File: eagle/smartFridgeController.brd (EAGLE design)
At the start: 39.7 x 25.4 mm, 8 parts

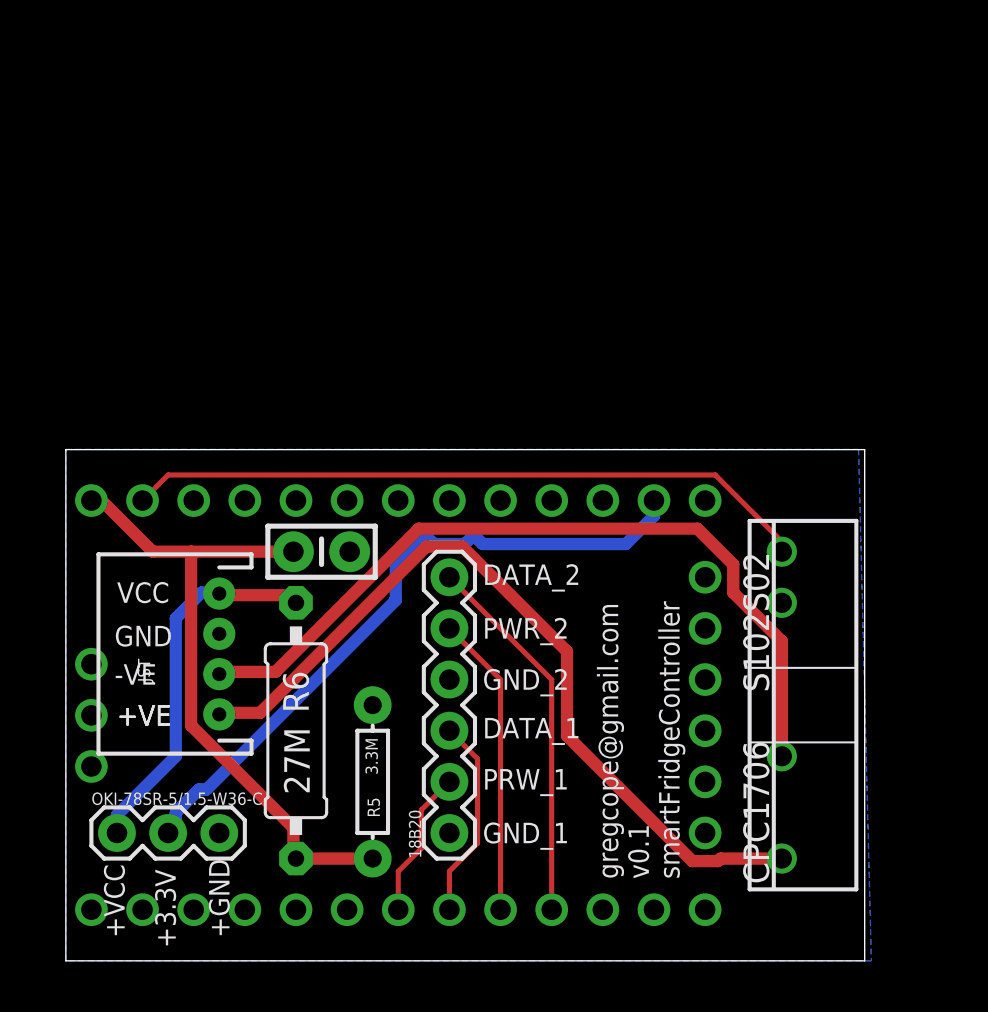
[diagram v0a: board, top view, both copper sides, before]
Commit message: added 3 LEDs
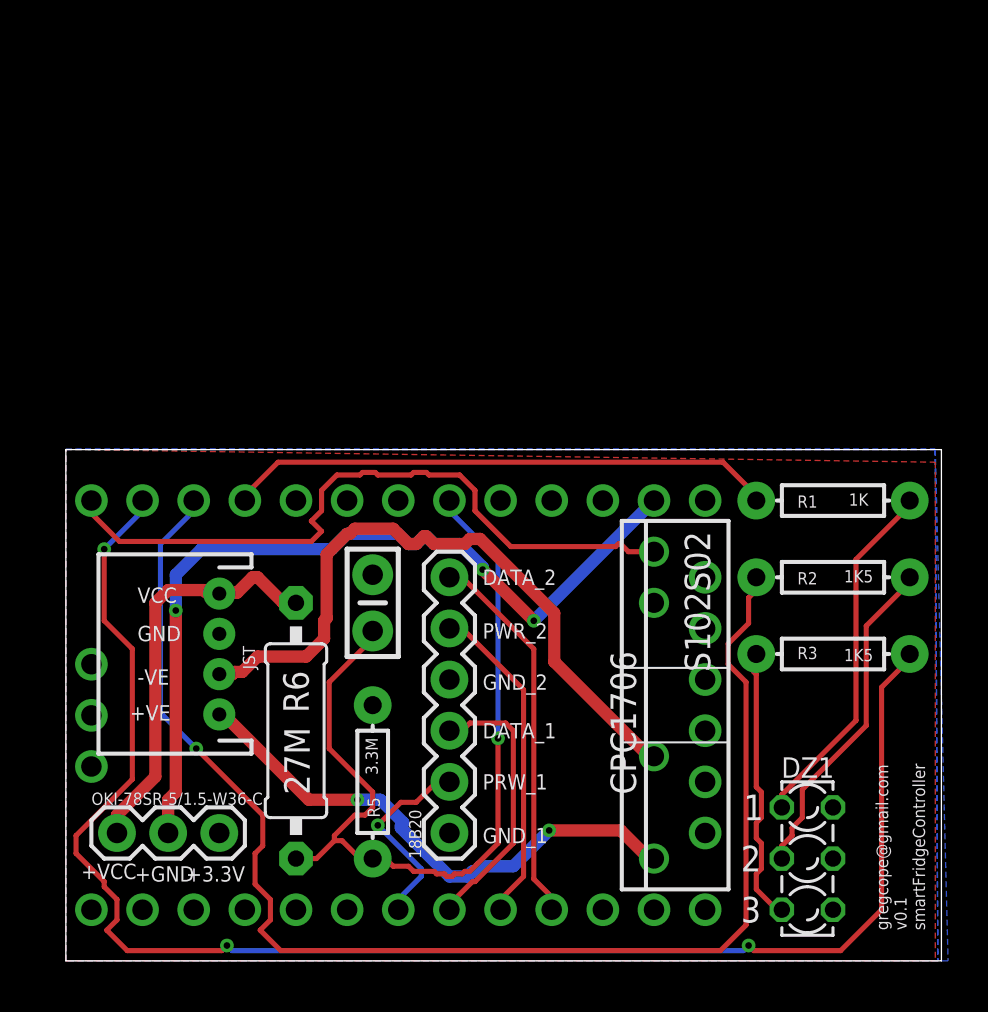
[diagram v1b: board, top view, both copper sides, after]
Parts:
- added DZ1: LZR183, led:LZR183
- added R1: 1K, SparkFun-Resistors:AXIAL-0.3
- added R2, R3: 1K5, SparkFun-Resistors:AXIAL-0.3
- moved CPC1706 6.35 mm to (29.2, 12.7)
- moved C2 3.59 mm to (15.2, 17.8), turned to 90 degrees
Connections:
- removed net A0_VCC_VD: C2.1, R5.P$2, R6.1, U$1.A0
- removed net D15_RELAY_PIN: CPC1706.4, U$1.A1
- new net A7_VCC_VD: C2.1, R5.P$2, R6.1, U$1.A7_ONLY
- new net D14_RELAY_PIN: CPC1706.4, U$1.A0
- new net D15_LED_RED_PIN: R3.P$2, U$1.A1
- new net D16_LED_YELLOW_PIN: R2.P$2, U$1.A2
- new net D17_LED_GREEN_PIN: R1.P$2, U$1.A3
- new net N$1: DZ1.A1, R1.P$1
- new net N$2: DZ1.A2, R2.P$1
- new net N$3: DZ1.A3, R3.P$1
- net GND: now also DZ1.K1, DZ1.K2, DZ1.K3
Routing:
- net D15_LED_RED_PIN: track 0.00 -> 78.4 mm, vias 0 -> 3
- net D16_LED_YELLOW_PIN: track 0.00 -> 68.1 mm, vias 0 -> 1
- net A7_VCC_VD: track 0.00 -> 43.1 mm, vias 0 -> 1
- net D14_RELAY_PIN: track 0.00 -> 34.6 mm
- net D15_RELAY_PIN: track 34.2 -> 0.00 mm
- net A0_VCC_VD: track 32.3 -> 0.00 mm
- net D17_LED_GREEN_PIN: track 0.00 -> 27.3 mm
- net N$1: track 0.00 -> 17.9 mm
- net N$2: track 0.00 -> 16.6 mm
- net N$3: track 0.00 -> 13.9 mm
- net +VE: track 40.4 -> 26.8 mm, vias 0 -> 2
- net VIN: track 33.5 -> 42.2 mm, vias 0 -> 3
- net -VE: track 39.8 -> 33.6 mm
- net D6_DS1_DATA: track 10.0 -> 13.8 mm
- net D7_DS1_PWR: track 7.40 -> 10.0 mm, vias 0 -> 1
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- added copper zone on layer 1, net GND
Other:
- board size 39.7 x 25.4 mm -> 43.5 x 25.4 mm

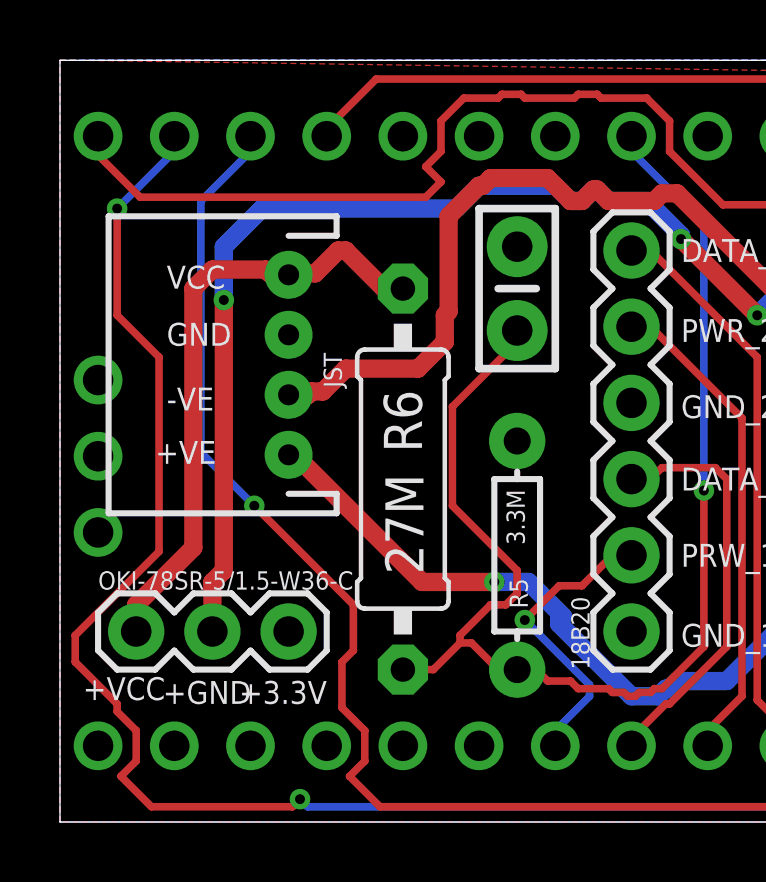
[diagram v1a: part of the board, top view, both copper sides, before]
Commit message: silkscreen updates
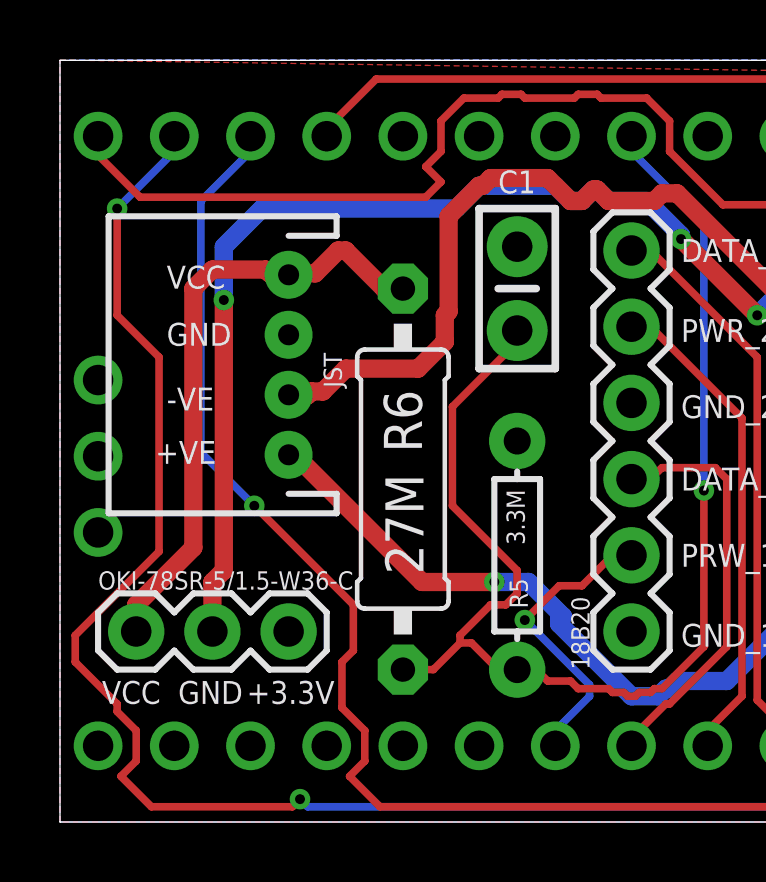
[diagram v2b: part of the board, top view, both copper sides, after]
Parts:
- renumbered C2 to C1
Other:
- board text added: "C1"
- board text removed: "+GND"
- board text removed: "+VCC"
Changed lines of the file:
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@@
 <text x="20.701" y="5.842" size="0.762" layer="25" font="vector">GND_1</text>
 <text x="3.175" y="11.938" size="0.762" layer="25" font="vector">+VE</text>
-<text x="0.762" y="4.064" size="0.762" layer="25" font="vector">+VCC</text>
-<text x="5.969" y="3.937" size="0.762" layer="25" font="vector">+3.3V</text>
-<text x="3.429" y="3.937" size="0.762" layer="25" font="vector">+GND</text>
+<text x="1.397" y="3.937" size="0.762" layer="25" font="vector">VCC</text>
+<text x="6.223" y="3.937" size="0.762" layer="25" font="vector">+3.3V</text>
+<text x="3.937" y="3.937" size="0.762" layer="25" font="vector">GND</text>
+<text x="14.605" y="20.955" size="0.762" layer="25" font="vector">C1</text>
 </plain>
 <attributes>
@@
 </autorouter>
 <elements>
-<element name="C2" library="SparkFun-Capacitors" package="CAP-PTH-SMALL-KIT" value="0.1U" x="15.24" y="17.78" smashed="yes" rot="R90">
+<element name="C1" library="SparkFun-Capacitors" package="CAP-PTH-SMALL-KIT" value="0.1U" x="15.24" y="17.78" smashed="yes" rot="R90">
 <attribute name="PROD_ID" value="CAP-08370" x="-11.43" y="6.35" size="1.778" layer="27" rot="R90" display="off"/>
 </element>
@@
 <vertex x="0" y="0"/>
 </polygon>
-<contactref element="C2" pad="2"/>
+<contactref element="C1" pad="2"/>
 <contactref element="R5" pad="P$1"/>
 <contactref element="JST" pad="3"/>
@@
 <signal name="A7_VCC_VD">
 <contactref element="U$1" pad="A7_ONLY"/>
-<contactref element="C2" pad="1"/>
+<contactref element="C1" pad="1"/>
 <contactref element="R5" pad="P$2"/>
 <contactref element="R6" pad="1"/>

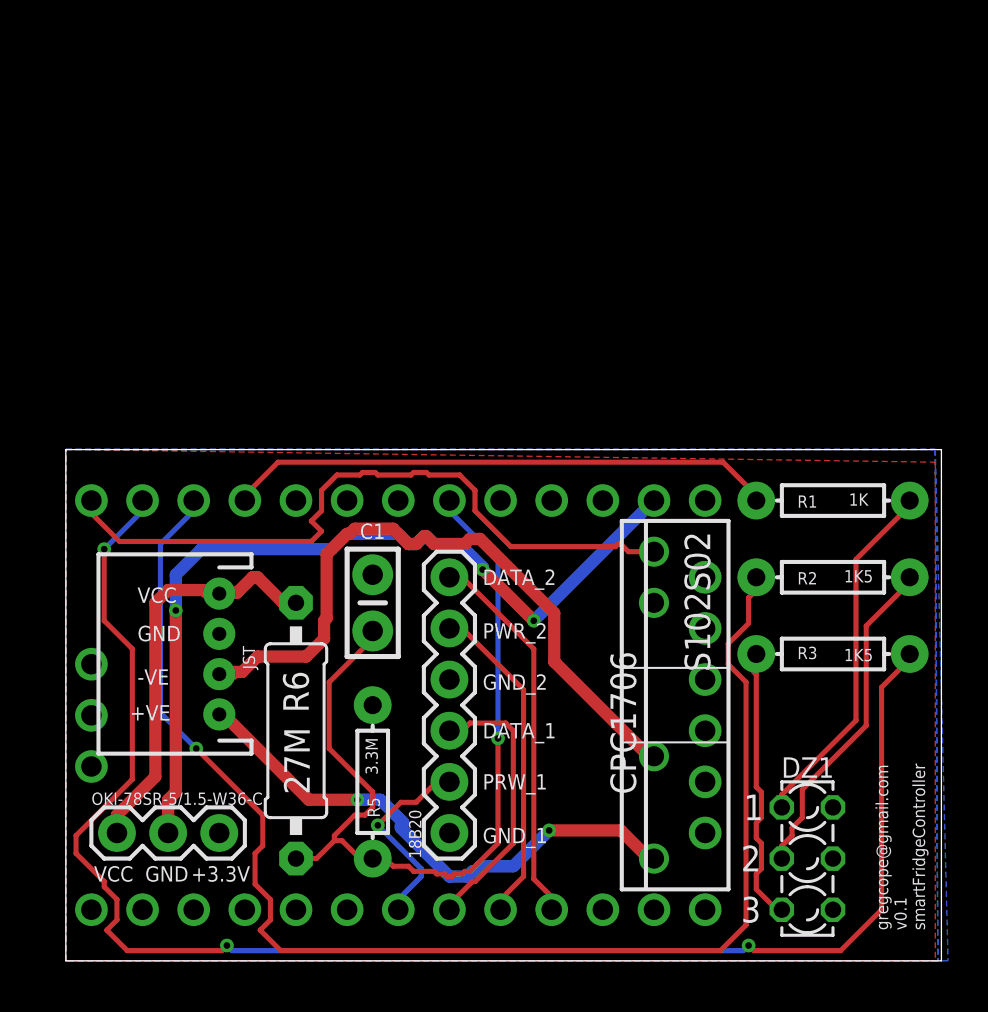
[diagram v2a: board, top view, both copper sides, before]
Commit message: Swapped IXYS pins
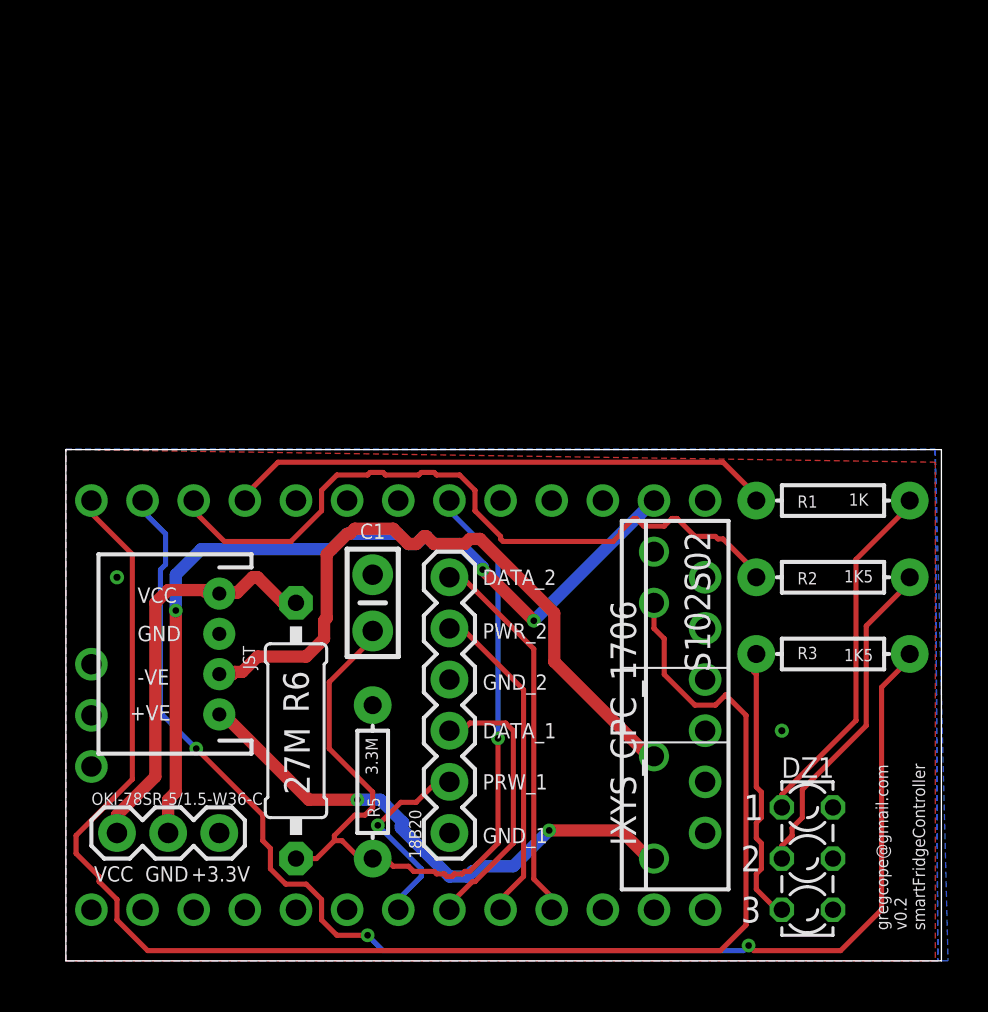
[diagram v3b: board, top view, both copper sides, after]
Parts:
- renumbered CPC1706 to IXYS_CPC_1706
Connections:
- net D14_RELAY_PIN: now also IXYS_CPC_1706.3; no longer IXYS_CPC_1706.4
- net GND: now also IXYS_CPC_1706.4; no longer IXYS_CPC_1706.3
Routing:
- net D14_RELAY_PIN: track 34.6 -> 75.6 mm
- net D16_LED_YELLOW_PIN: track 68.1 -> 35.5 mm, vias 1 -> 0
- net D15_LED_RED_PIN: track 78.4 -> 68.1 mm
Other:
- board text added: "gregcope@gmail.com v0.2 smartFridgeController"
- board text removed: "gregcope@gmail.com v0.1 smartFridgeController"

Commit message: Correct SIP package, large footprint
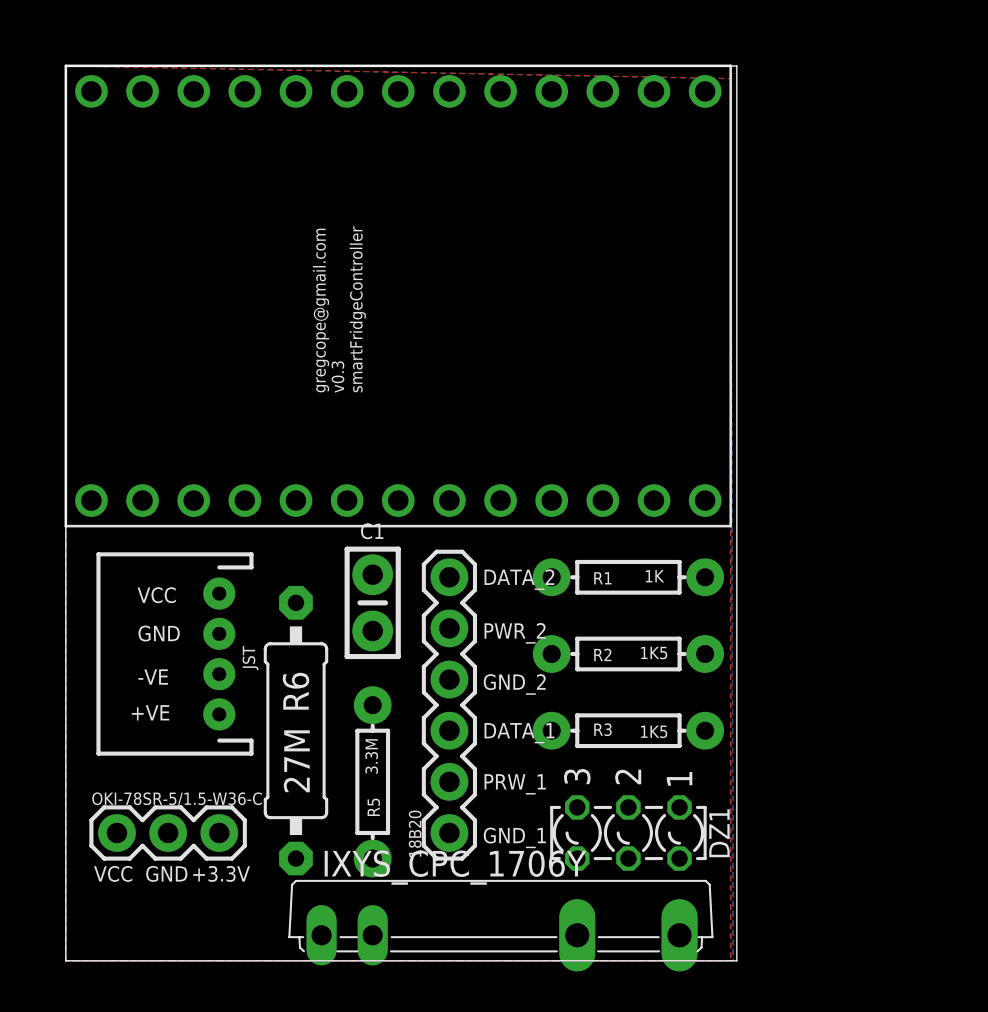
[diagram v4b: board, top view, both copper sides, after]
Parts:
- removed IXYS_CPC_1706: S102S02, relay:S202S02
- removed U$1: MOTEINOR6, Moteino:MOTEINO_R6
- added IXYS_CPC_1706Y: AQZ102D, relay:AQZ-SIL04
- added U$2: MOTEINO_SIMPLE, Moteino:MOTEINO_SIMPLE
- moved R1 10.9 mm to (27.9, 19.1)
- moved R2 10.9 mm to (27.9, 15.2)
- moved R3 10.9 mm to (27.9, 11.4)
- moved DZ1 8.98 mm to (27.9, 6.35), turned to 270 degrees
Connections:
- net +VE: now also IXYS_CPC_1706Y.4; no longer IXYS_CPC_1706.1
- net -VE: now also IXYS_CPC_1706Y.3; no longer IXYS_CPC_1706.2
- net A7_VCC_VD: now also U$2.A7_ONLY; no longer U$1.A7_ONLY
- net D14_RELAY_PIN: now also IXYS_CPC_1706Y.2, U$2.A0; no longer IXYS_CPC_1706.3, U$1.A0
- net D15_LED_RED_PIN: now also U$2.A1; no longer U$1.A1
- net D16_LED_YELLOW_PIN: now also U$2.A2; no longer U$1.A2
- net D17_LED_GREEN_PIN: now also U$2.A3; no longer U$1.A3
- net D4_DS2_DATA: now also U$2.D4; no longer U$1.D4
- net D5_DS2_PWR: now also U$2.D5; no longer U$1.D5
- net D6_DS1_DATA: now also U$2.D6; no longer U$1.D6
- net D7_DS1_PWR: now also U$2.D7; no longer U$1.D7
- net GND: now also IXYS_CPC_1706Y.1, U$2.GND1; no longer IXYS_CPC_1706.4
- net VIN: now also U$2.VIN; no longer U$1.VIN
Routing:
- net D14_RELAY_PIN: track 75.6 -> 0.00 mm
- net D15_LED_RED_PIN: track 68.1 -> 0.00 mm, vias 3 -> 0
- net A7_VCC_VD: track 43.1 -> 0.00 mm, vias 1 -> 0
- net VIN: track 42.2 -> 0.00 mm, vias 3 -> 0
- net D16_LED_YELLOW_PIN: track 35.5 -> 0.00 mm
- net -VE: track 33.6 -> 0.00 mm
- net D17_LED_GREEN_PIN: track 27.3 -> 0.00 mm
- net +VE: track 26.8 -> 0.00 mm, vias 2 -> 0
- net VCC: track 20.4 -> 0.00 mm
- net D4_DS2_DATA: track 19.0 -> 0.00 mm
- net N$1: track 17.9 -> 0.00 mm
- net N$2: track 16.6 -> 0.00 mm
- net D5_DS2_PWR: track 16.3 -> 0.00 mm
- net N$3: track 13.9 -> 0.00 mm
- net D6_DS1_DATA: track 13.8 -> 0.00 mm
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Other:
- board size 43.5 x 25.4 mm -> 33.3 x 44.4 mm
- board text added: "gregcope@gmail.com v0.3 smartFridgeController"
- board text removed: "gregcope@gmail.com v0.2 smartFridgeController"

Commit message: Added gititgnore
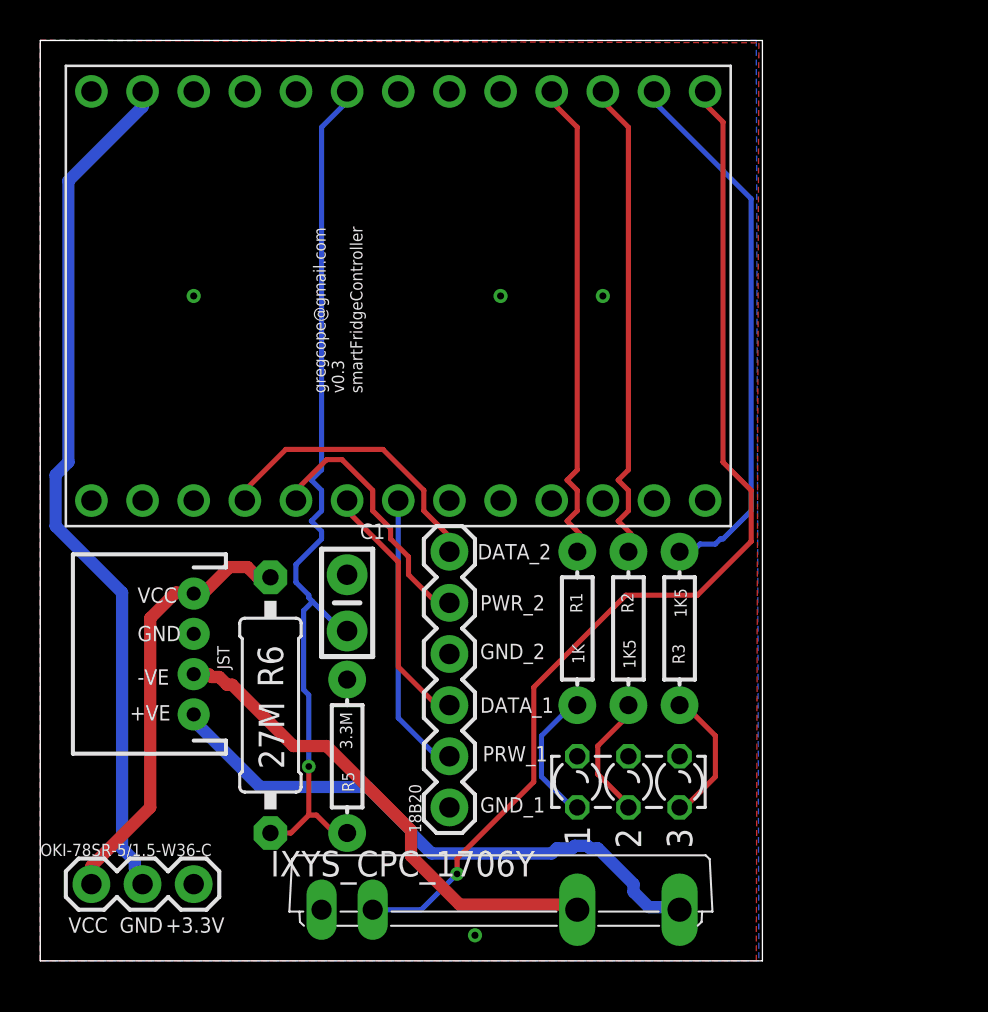
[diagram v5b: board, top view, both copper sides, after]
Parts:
- 18B20: value (none) -> JST
- moved R3 5.68 mm to (30.5, 16.5), turned to 90 degrees
- moved R1 3.59 mm to (25.4, 16.5), turned to 90 degrees
- moved OKI-78SR-5/1.5-W36-C 2.84 mm to (1.27, 3.81)
- moved DZ1 2.54 mm to (27.9, 8.89), turned to 90 degrees
- moved R5 1.80 mm to (14.0, 10.2)
- moved R6 1.80 mm to (10.2, 12.7)
- moved R2 1.27 mm to (27.9, 16.5), turned to 90 degrees
- moved 18B20 1.27 mm to (19.1, 7.62)
- moved JST 1.27 mm to (6.35, 15.2)
- moved IXYS_CPC_1706Y 1.27 mm to (21.6, 2.54)
- moved C1 1.27 mm to (14.0, 17.8)
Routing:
- net D14_RELAY_PIN: track 0.00 -> 52.9 mm, vias 0 -> 1
- net A7_VCC_VD: track 0.00 -> 45.3 mm, vias 0 -> 1
- net VIN: track 0.00 -> 42.9 mm
- net +VE: track 0.00 -> 28.9 mm
- net D15_LED_RED_PIN: track 0.00 -> 27.2 mm
- net -VE: track 0.00 -> 24.6 mm
- net D16_LED_YELLOW_PIN: track 0.00 -> 24.3 mm
- net D17_LED_GREEN_PIN: track 0.00 -> 24.3 mm
- net VCC: track 0.00 -> 21.7 mm
- net D4_DS2_DATA: track 0.00 -> 14.7 mm
- net D7_DS1_PWR: track 0.00 -> 14.1 mm
- net D5_DS2_PWR: track 0.00 -> 13.1 mm
- net D6_DS1_DATA: track 0.00 -> 12.6 mm
- net N$3: track 0.00 -> 6.85 mm
- net N$1: track 0.00 -> 6.85 mm
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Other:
- board size 33.3 x 44.4 mm -> 35.9 x 45.7 mm
